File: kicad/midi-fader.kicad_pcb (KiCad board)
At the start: 2 copper layers, 73.7 x 78.7 mm, 57 parts, among them J1 SWD, J2 EXTERNAL_OUT, J3 EXTERNAL_IN, J4 USB_OTG, U1 STM32F042FxP, U2 USBLC6-2, U3 MCP1603, U4 MIC2776L, U5 MIC5501-XYM5

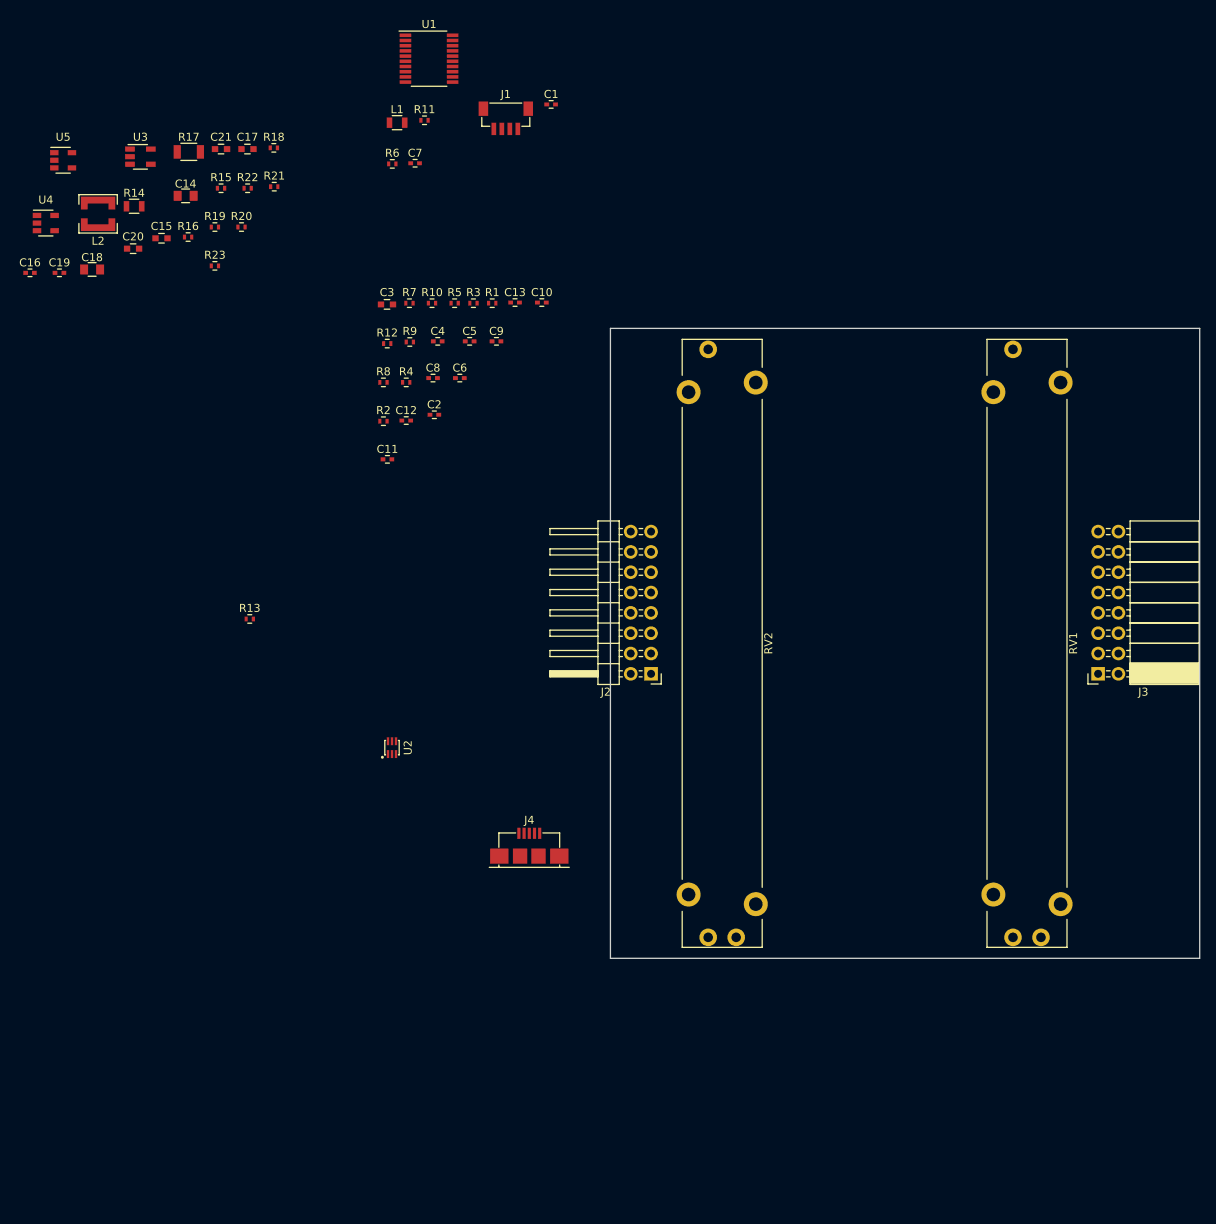
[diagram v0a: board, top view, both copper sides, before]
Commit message: Changed microcontroller to 32-LQFP variety
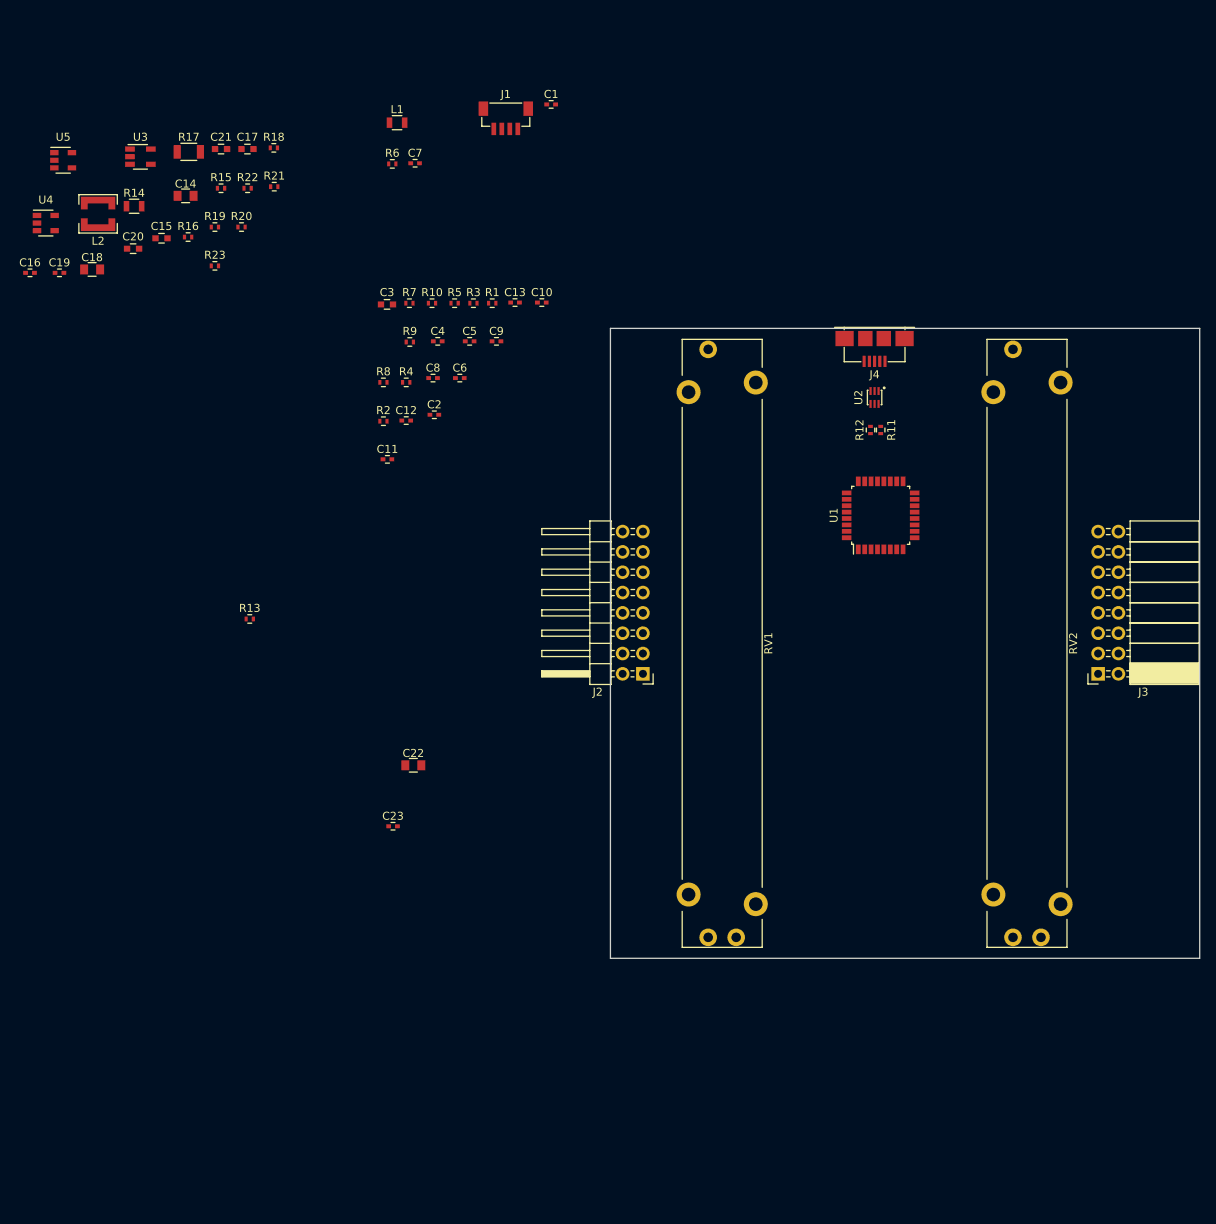
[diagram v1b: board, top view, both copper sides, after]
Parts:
- added C22: 4.7u, Capacitors_SMD:C_0805, F.Cu at (92.2, 118.1)
- added C23: 0.1u, Capacitors_SMD:C_0402, F.Cu at (89.7, 125.7)
- U1: value STM32F042FxP -> STM32F042KxT; footprint Housings_SSOP:TSSOP-20_4.4x6.5mm_Pitch0.65mm -> Housings_QFP:LQFP-32_7x7mm_Pitch0.8mm
- moved U1 80.3 mm to (150.6, 86.9), turned to 90 degrees
- moved J4 77.8 mm to (149.9, 64.8), turned to 180 degrees
- moved U2 74.5 mm to (149.9, 72.1), turned to 180 degrees
- moved R11 68.9 mm to (150.6, 76.2), turned to 270 degrees
- moved R12 61.4 mm to (149.4, 76.2), turned to 90 degrees
- moved RV1 38.1 mm to (130.8, 102.9)
- moved RV2 38.1 mm to (168.9, 102.9)
- moved J2 1.02 mm to (120.9, 106.7)
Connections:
- RV1 pad 1: VDDA -> GND
- RV1 pad 3: GND -> VDDA
- RV2 pad 1: VDDA -> GND
- RV2 pad 3: GND -> VDDA
- U1 pad 1: GND -> VDD
- U1 pad 15: GND -> Net-(U1-Pad15)
- U1 pad 16: VDD -> GND
- U1 pad 17: /Digital Control/USB_R- -> VDD
- U1 pad 18: /Digital Control/USB_R+ -> Net-(U1-Pad18)
- U1 pad 19: /Digital Control/SWDIO -> Net-(U1-Pad19)
- U1 pad 20: /Digital Control/SWCLK -> Net-(U1-Pad20)
- U2 pad 1: /Digital Control/USB_TVS_D+ -> /Digital Control/USB_TVS_D-
- U2 pad 3: /Digital Control/USB_TVS_D- -> /Digital Control/USB_TVS_D+
- U2 pad 4: /Digital Control/USB_D- -> /Digital Control/USB_D+
- U2 pad 6: /Digital Control/USB_D+ -> /Digital Control/USB_D-

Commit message: Completed initial placement
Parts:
- C1, C10, C11, C12, C13, C14, C16, C17, C18, C19, C2, C23, C4, C5, C6, C7, C8, C9, J1, J4, L1, L2, R1, R10, R11, R12, R13, R14, R15, R17, R18, R2, R21, R23, R3, R4, R5, R6, R7, R8, R9, U1, U2, U3, U4: moved to B.Cu
- moved C16 102.4 mm to (142.5, 85.6), turned to 90 degrees
- moved U5 101.7 mm to (144.8, 74.9), turned to 270 degrees
- moved C18 98.5 mm to (146.1, 85.6), turned to 90 degrees
- moved L2 94.8 mm to (139.0, 88.5), turned to 270 degrees
- moved R17 94.0 mm to (143.3, 92.3), turned to 270 degrees
- moved R6 92.9 mm to (166.4, 95.2)
- moved U4 92.9 mm to (133.3, 82.5), turned to 90 degrees
- moved R13 92.2 mm to (157.7, 66.5), turned to 270 degrees
- moved C20 91.1 mm to (144.8, 78.5), turned to 180 degrees
- moved L1 91.1 mm to (169.9, 81.8), turned to 180 degrees
- moved U3 90.9 mm to (139.4, 82.6), turned to 270 degrees
- moved C19 89.2 mm to (134.1, 79.5), turned to 180 degrees
- moved C7 87.8 mm to (163.8, 94.0), turned to 180 degrees
- moved C15 86.7 mm to (145.3, 71.4), turned to 180 degrees
- moved R14 86.4 mm to (139.4, 74.9)
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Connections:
- net Net-(L2-Pad1) renamed /Power Supplies/VDD_L
- net Net-(R15-Pad2) renamed /Power Supplies/VDD_EN_SENSE
- net Net-(R16-Pad2) renamed /Power Supplies/~VDD_SHDN
- net Net-(R20-Pad2) renamed /Power Supplies/VDDA_EN
- net Net-(R21-Pad2) renamed /Power Supplies/VDD_EN_MR
- J3 pad 1: GND -> VDDA
- J3 pad 10: /Digital Control/IN2 -> /Digital Control/IN3
- J3 pad 11: /Digital Control/IN5 -> /Digital Control/IN4
- J3 pad 12: /Digital Control/IN4 -> /Digital Control/IN5
- J3 pad 15: GND -> VDD
- J3 pad 16: VDD -> GND
- J3 pad 2: VDDA -> GND
- J3 pad 7: /Digital Control/IN1 -> /Digital Control/IN0
- J3 pad 8: /Digital Control/IN0 -> /Digital Control/IN1
- J3 pad 9: /Digital Control/IN3 -> /Digital Control/IN2

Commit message: Initial routing complete
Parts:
- added REF**: 1PIN_VIA, midi-fader:1PIN_VIA, F.Cu at (168.8, 77.6)
- added REF**: 1PIN_VIA, midi-fader:1PIN_VIA, F.Cu at (146.4, 89.9)
- added REF**: 1PIN_VIA, midi-fader:1PIN_VIA, F.Cu at (146.4, 88.9)
- added REF**: 1PIN_VIA, midi-fader:1PIN_VIA, F.Cu at (146.4, 87.9)
- added REF**: 1PIN_VIA, midi-fader:1PIN_VIA, F.Cu at (170.7, 76.6)
- added REF**: 1PIN_VIA, midi-fader:1PIN_VIA, F.Cu at (172.7, 76.7)
- added REF**: 1PIN_VIA, midi-fader:1PIN_VIA, F.Cu at (131.2, 80.4)
- added REF**: 1PIN_VIA, midi-fader:1PIN_VIA, F.Cu at (134.2, 80.4)
- added REF**: 1PIN_VIA, midi-fader:1PIN_VIA, F.Cu at (146.3, 69.6)
- added REF**: 1PIN_VIA, midi-fader:1PIN_VIA, F.Cu at (145.3, 69.6)
- added REF**: 1PIN_VIA, midi-fader:1PIN_VIA, F.Cu at (144.3, 69.6)
- added REF**: 1PIN_VIA, midi-fader:1PIN_VIA, F.Cu at (168.8, 78.5)
- added REF**: 1PIN_VIA, midi-fader:1PIN_VIA, F.Cu at (143.3, 69.6)
- added REF**: 1PIN_VIA, midi-fader:1PIN_VIA, F.Cu at (142.2, 69.6)
- added REF**: 1PIN_VIA, midi-fader:1PIN_VIA, F.Cu at (146.3, 68.6)
- added REF**: 1PIN_VIA, midi-fader:1PIN_VIA, F.Cu at (143.8, 72.5)
- added REF**: 1PIN_VIA, midi-fader:1PIN_VIA, F.Cu at (144.7, 72.5)
- added REF**: 1PIN_VIA, midi-fader:1PIN_VIA, F.Cu at (151.1, 73.2)
- added REF**: 1PIN_VIA, midi-fader:1PIN_VIA, F.Cu at (151.3, 71.1)
- added REF**: 1PIN_VIA, midi-fader:1PIN_VIA, F.Cu at (151.3, 70.2)
- added REF**: 1PIN_VIA, midi-fader:1PIN_VIA, F.Cu at (147.8, 74.2)
- added REF**: 1PIN_VIA, midi-fader:1PIN_VIA, F.Cu at (147.8, 72.9)
- added REF**: 1PIN_VIA, midi-fader:1PIN_VIA, F.Cu at (152.4, 84.8)
- added REF**: 1PIN_VIA, midi-fader:1PIN_VIA, F.Cu at (148.0, 71.5)
- added REF**: 1PIN_VIA, midi-fader:1PIN_VIA, F.Cu at (148.0, 70.5)
- added REF**: 1PIN_VIA, midi-fader:1PIN_VIA, F.Cu at (148.6, 69.7)
- added REF**: 1PIN_VIA, midi-fader:1PIN_VIA, F.Cu at (150.7, 69.3)
- added REF**: 1PIN_VIA, midi-fader:1PIN_VIA, F.Cu at (151.0, 72.1)
- added REF**: 1PIN_VIA, midi-fader:1PIN_VIA, F.Cu at (149.5, 74.3)
- added REF**: 1PIN_VIA, midi-fader:1PIN_VIA, F.Cu at (152.4, 84.1)
- added REF**: 1PIN_VIA, midi-fader:1PIN_VIA, F.Cu at (153.7, 87.8)
- added REF**: 1PIN_VIA, midi-fader:1PIN_VIA, F.Cu at (154.9, 86.7)
- added REF**: 1PIN_VIA, midi-fader:1PIN_VIA, F.Cu at (152.4, 86.7)
- added REF**: 1PIN_VIA, midi-fader:1PIN_VIA, F.Cu at (145.4, 90.9)
- added REF**: 1PIN_VIA, midi-fader:1PIN_VIA, F.Cu at (146.4, 90.9)
- C3: moved to B.Cu
- moved C12 8.89 mm to (163.8, 91.4)
- moved C5 8.89 mm to (163.8, 100.3)
- moved R1 8.89 mm to (166.4, 100.3)
- moved R10 8.89 mm to (166.4, 91.4)
- moved C11 6.35 mm to (163.8, 92.7)
- moved C6 6.35 mm to (163.8, 99.1)
- moved R3 6.35 mm to (166.4, 99.1)
- moved R9 6.35 mm to (166.4, 92.7)
- moved J1 4.58 mm to (157.7, 74.2), turned to 0 degrees
- moved C10 3.81 mm to (163.8, 94.0)
- moved C7 3.81 mm to (163.8, 97.8)
- moved R5 3.81 mm to (166.4, 97.8)
- moved R8 3.81 mm to (166.4, 94.0)
- moved C3 2.81 mm to (167.6, 81.3)
- moved C21 1.66 mm to (146.4, 80.4), turned to 0 degrees
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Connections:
- net Net-(C13-Pad1) renamed /Digital Control/CHSGND
- net Net-(C3-Pad1) renamed /Digital Control/VDDA_UC
- net Net-(L1-Pad1) renamed /Digital Control/VDDA_UC_PREFILT
- J2 pad 1: VDDA -> VDD
- J2 pad 15: VDD -> VDDA
- J3 pad 1: VDDA -> VDD
- J3 pad 15: VDD -> VDDA
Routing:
- net /Digital Control/FADER_A: track 0.00 -> 115.1 mm, vias 0 -> 3
- net /Digital Control/FADER_B: track 0.00 -> 110.6 mm, vias 0 -> 2
- net /Digital Control/IN1: track 0.00 -> 71.3 mm, vias 0 -> 2
- net /Digital Control/IN3: track 0.00 -> 69.9 mm, vias 0 -> 2
- net /Digital Control/IN0: track 0.00 -> 65.6 mm, vias 0 -> 2
- net /Digital Control/IN2: track 0.00 -> 64.6 mm, vias 0 -> 2
- net /Digital Control/ANALOG_IN0: track 0.00 -> 27.1 mm, vias 0 -> 2
- net /Digital Control/ANALOG_IN1: track 0.00 -> 25.3 mm, vias 0 -> 2
- net /Digital Control/ANALOG_IN2: track 0.00 -> 21.6 mm, vias 0 -> 2
- net /Digital Control/ANALOG_IN3: track 0.00 -> 18.6 mm, vias 0 -> 2
- net /Digital Control/ANALOG_IN4: track 0.00 -> 16.7 mm, vias 0 -> 2
- net /Digital Control/IN5: track 0.00 -> 14.6 mm
- net /Digital Control/NRST: track 0.00 -> 13.2 mm, vias 0 -> 2
- net /Power Supplies/~VDD_SHDN: track 0.00 -> 12.5 mm, vias 0 -> 1
- net /Digital Control/ANALOG_IN5: track 0.00 -> 12.3 mm, vias 0 -> 2
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- added copper zone on B.Cu, net /Digital Control/CHSGND
- added copper zone on B.Cu, net /Digital Control/VDDA_UC
- added copper zone on F.Cu, net /Digital Control/VDDA_UC_PREFILT
- added copper zone on B.Cu, net /Power Supplies/VDD_L
- added copper zone on B.Cu, net GND
- added copper zone on F.Cu, net GND
- added copper zone on B.Cu, net VBUS
- added copper zone on F.Cu, net VBUS
- added copper zone on B.Cu, net VDD
- added copper zone on F.Cu, net VDD
- added copper zone on B.Cu, net VDDA
- added copper zone on F.Cu, net VDDA
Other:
- net class Default: clearance 0.2 -> 0.1524; trace_width 0.25 -> 0.254; via_dia 0.6 -> 1; via_drill 0.4 -> 0.6
- net class USB added: clearance 0.1524, trace_width 0.1524, via_dia 1, via_drill 0.6
- rule pad_to_mask_clearance: 0.2 -> 0.1524
- rule trace_clearance: 0.2 -> 0.1524
- rule trace_min: 0.2 -> 0.1524
- rule via_min_size: 0.4 -> 0.6
